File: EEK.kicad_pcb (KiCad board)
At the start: 2 copper layers, 165 x 51.8 mm, 35 parts

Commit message: add PCB features
Add PCB deatures un PCB Editor
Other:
- board text added: "0,0000 mm / 0,0000 mm"
- board text added: "0,3000 mm"
- board text added: "1,6000 mm"
- board text added: "165,0000 mm x 51,7500 mm"
- board text added: "2"
- board text added: "CARACTÉRISTIQUES du PCB"
- board text added: "Connecteurs de bord de cartes:"
- board text added: "Contour du PCB Métallisé:"
- board text added: "Contrôle d'Impédance:"
- board text added: "Diamètre de trou min:"
- board text added: "Dimensions hors tout PCB:"
- board text added: "Epaisseur du PCB:"
- board text added: "Finition Cuivre:"
- board text added: "Nombre de Couches Cuivre:"
- board text added: "Non"
- board text added: "None"
- board text added: "Pads castellated:"
- board text added: "Piste / espacement min:"

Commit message: fix the bug on OLED power supply pin1 and 2 inverted (3.3V and GND)
Fix the bug on the OLED power supply pins which have been inverted PIN 1 3.3V and pin 2 GND
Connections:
- U10 pad 1: GND -> /3.3V
- U10 pad 2: /3.3V -> GND
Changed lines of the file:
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@@
 			)
 		)
+		(sheetname "Racine")
+		(sheetfile "EEK.kicad_sch")
 		(attr through_hole)
 		(fp_line
@@
 			)
 		)
+		(property ki_fp_filters "R_*")
+		(sheetname "Racine")
+		(sheetfile "EEK.kicad_sch")
 		(attr through_hole)
 		(fp_line
@@
 			)
 		)
+		(property ki_fp_filters "Pin* Test*")
+		(sheetname "Racine")
+		(sheetfile "EEK.kicad_sch")
 		(attr exclude_from_pos_files)
 		(fp_circle
@@
 			)
 		)
+		(property ki_fp_filters "Pin* Test*")
+		(sheetname "Racine")
+		(sheetfile "EEK.kicad_sch")
 		(attr exclude_from_pos_files)
 		(fp_circle
@@
 			)
 		)
+		(property ki_fp_filters "LED* LED_SMD:* LED_THT:*")
+		(sheetname "Racine")
+		(sheetfile "EEK.kicad_sch")
 		(attr through_hole)
 		(fp_line
@@
 			)
 		)
+		(property ki_fp_filters "Pin* Test*")
+		(sheetname "Racine")
+		(sheetfile "EEK.kicad_sch")
 		(attr exclude_from_pos_files)
 		(fp_circle
@@
 			)
 		)
+		(property ki_fp_filters "R_*")
+		(sheetname "Racine")
+		(sheetfile "EEK.kicad_sch")
 		(attr through_hole)
 		(fp_line
@@
 			)
 		)
+		(property ki_fp_filters "LED* LED_SMD:* LED_THT:*")
+		(sheetname "Racine")
+		(sheetfile "EEK.kicad_sch")
 		(attr through_hole)
 		(fp_line
@@
 			)
 		)
+		(property ki_fp_filters "Pin* Test*")
+		(sheetname "Racine")
+		(sheetfile "EEK.kicad_sch")
 		(attr exclude_from_pos_files)
 		(fp_circle
@@
 			)
 		)
+		(sheetname "Racine")
+		(sheetfile "EEK.kicad_sch")
 		(attr through_hole)
 		(fp_rect
@@
 			)
 		)
+		(sheetname "Racine")
+		(sheetfile "EEK.kicad_sch")
 		(attr through_hole)
 		(fp_line
@@
 			(layers "*.Cu" "*.Mask")
 			(remove_unused_layers no)
-			(net 49 "GND")
-			(pinfunction "GND")
+			(net 26 "/3.3V")
+			(pinfunction "VDD")
 			(pintype "passive")
 		)
@@
 			(layers "*.Cu" "*.Mask")
 			(remove_unused_layers no)
-			(net 26 "/3.3V")
-			(pinfunction "VDD")
+			(net 49 "GND")
+			(pinfunction "GND")
 			(pintype "passive")
 		)
@@
 			)
 		)
+		(property ki_fp_filters "LED* LED_SMD:* LED_THT:*")
+		(sheetname "Racine")
+		(sheetfile "EEK.kicad_sch")
 		(attr through_hole)
 		(fp_line
@@
 			)
 		)
+		(property ki_fp_filters "Pin* Test*")
+		(sheetname "Racine")
+		(sheetfile "EEK.kicad_sch")
 		(attr exclude_from_pos_files)
 		(fp_circle
@@
 			)
 		)
+		(property ki_fp_filters "LED* LED_SMD:* LED_THT:*")
+		(sheetname "Racine")
+		(sheetfile "EEK.kicad_sch")
 		(attr through_hole)
 		(fp_line
@@
 			)
 		)
+		(property ki_fp_filters "LED* LED_SMD:* LED_THT:*")
+		(sheetname "Racine")
+		(sheetfile "EEK.kicad_sch")
 		(attr through_hole)
 		(fp_line
@@
 			)
 		)
+		(property ki_fp_filters "Pin* Test*")
+		(sheetname "Racine")
+		(sheetfile "EEK.kicad_sch")
 		(attr exclude_from_pos_files)
 		(fp_circle
@@
 			)
 		)
+		(property ki_fp_filters "Pin* Test*")
+		(sheetname "Racine")
+		(sheetfile "EEK.kicad_sch")
 		(attr exclude_from_pos_files)
 		(fp_circle
@@
 			)
 		)
+		(property ki_fp_filters "Pin* Test*")
+		(sheetname "Racine")
+		(sheetfile "EEK.kicad_sch")
 		(attr exclude_from_pos_files)
 		(fp_circle
@@
 			)
 		)
+		(sheetname "Racine")
+		(sheetfile "EEK.kicad_sch")
 		(attr through_hole)
 		(fp_line
@@
 			)
 		)
+		(property ki_fp_filters "LED* LED_SMD:* LED_THT:*")
+		(sheetname "Racine")
+		(sheetfile "EEK.kicad_sch")
 		(attr through_hole)
 		(fp_line
@@
 			)
 		)
+		(sheetname "Racine")
+		(sheetfile "EEK.kicad_sch")
 		(attr through_hole)
 		(fp_line
@@
 			)
 		)
+		(sheetname "Racine")
+		(sheetfile "EEK.kicad_sch")
 		(attr through_hole)
 		(fp_line
@@
 			)
 		)
+		(property ki_fp_filters "Pin* Test*")
+		(sheetname "Racine")
+		(sheetfile "EEK.kicad_sch")
 		(attr exclude_from_pos_files)
 		(fp_circle
@@
 			)
 		)
+		(sheetname "Racine")
+		(sheetfile "EEK.kicad_sch")
 		(attr through_hole)
 		(fp_line
@@
 			)
 		)
+		(property ki_fp_filters "Pin* Test*")
+		(sheetname "Racine")
+		(sheetfile "EEK.kicad_sch")
 		(attr exclude_from_pos_files)
 		(fp_circle
@@
 			)
 		)
+		(property ki_fp_filters "R_*")
+		(sheetname "Racine")
+		(sheetfile "EEK.kicad_sch")
 		(attr through_hole)
 		(fp_line
@@
 			)
 		)
+		(property ki_fp_filters "R_*")
+		(sheetname "Racine")
+		(sheetfile "EEK.kicad_sch")
 		(attr through_hole)
 		(fp_line
@@
 			)
 		)
+		(property ki_fp_filters "Pin* Test*")
+		(sheetname "Racine")
+		(sheetfile "EEK.kicad_sch")
 		(attr exclude_from_pos_files)
 		(fp_circle
@@
 			)
 		)
+		(property ki_fp_filters "R_*")
+		(sheetname "Racine")
+		(sheetfile "EEK.kicad_sch")
 		(attr through_hole)
 		(fp_line
@@
 			)
 		)
+		(property ki_fp_filters "Pin* Test*")
+		(sheetname "Racine")
+		(sheetfile "EEK.kicad_sch")
 		(attr exclude_from_pos_files)
 		(fp_circle
@@
 			)
 		)
+		(sheetname "Racine")
+		(sheetfile "EEK.kicad_sch")
 		(attr through_hole)
 		(fp_line
@@
 			)
 		)
+		(property ki_fp_filters "R_*")
+		(sheetname "Racine")
+		(sheetfile "EEK.kicad_sch")
 		(attr through_hole)
 		(fp_line
@@
 			)
 		)
+		(sheetname "Racine")
+		(sheetfile "EEK.kicad_sch")
 		(attr through_hole)
 		(fp_line
@@
 			)
 		)
+		(property ki_fp_filters "Pin* Test*")
+		(sheetname "Racine")
+		(sheetfile "EEK.kicad_sch")
 		(attr exclude_from_pos_files)
 		(fp_circle

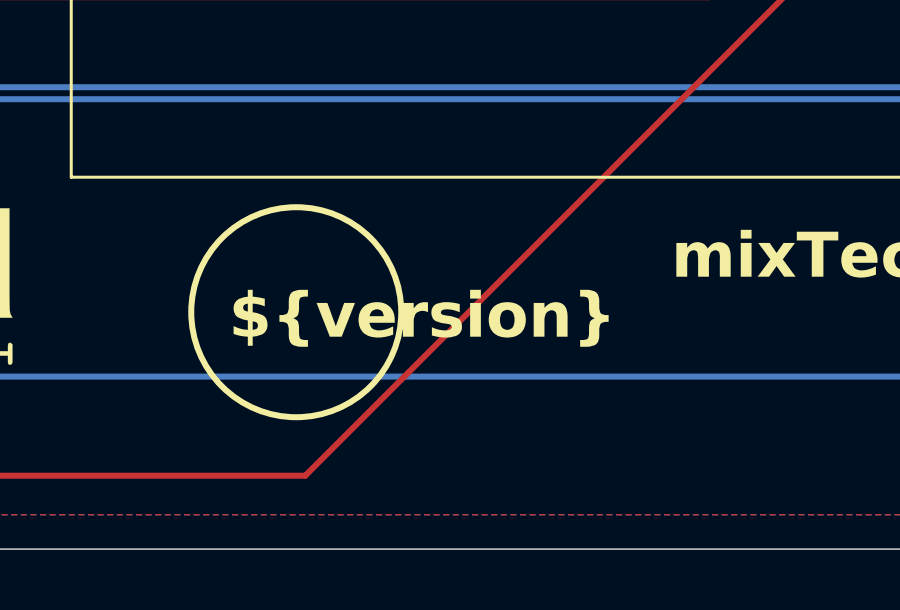
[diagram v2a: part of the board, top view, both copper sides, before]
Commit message: update version number V1.1
update version number to 1.1
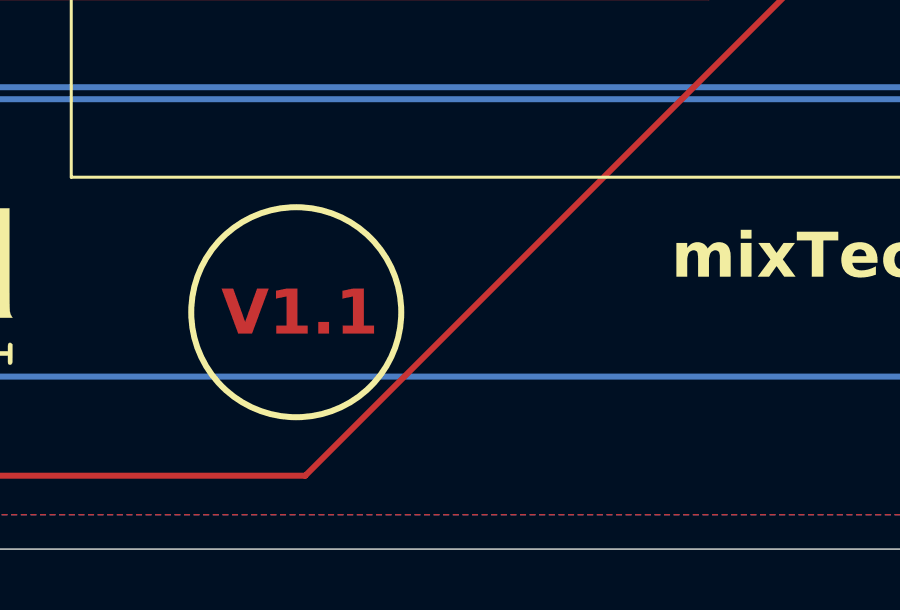
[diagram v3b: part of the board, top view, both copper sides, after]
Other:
- board text added: "V1.1"
- board text removed: "${version}"
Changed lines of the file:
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@@
 	(property "compagny" "mixTech")
 	(property "title" "PCB EEK for ESP32-WROOM-32")
-	(property "version" "V1.0")
+	(property "version" "V1.1")
 	(net 0 "")
 	(net 1 "/GFL")
@@
 		(layer "Edge.Cuts")
 	)
+	(gr_text "V1.1"
+		(at 146.25 121.5 0)
+		(layer "F.Cu")
+		(effects
+			(font
+				(size 1.5 1.5)
+				(thickness 0.3)
+				(bold yes)
+			)
+			(justify left bottom)
+		)
+	)
 	(gr_text "-"
 		(at 94.25 101.6041 0)
@@
 		)
 	)
-	(gr_text "${version}"
+	(gr_text "\n\n"
 		(at 146.5 121.6041 0)
 		(layer "F.SilkS")

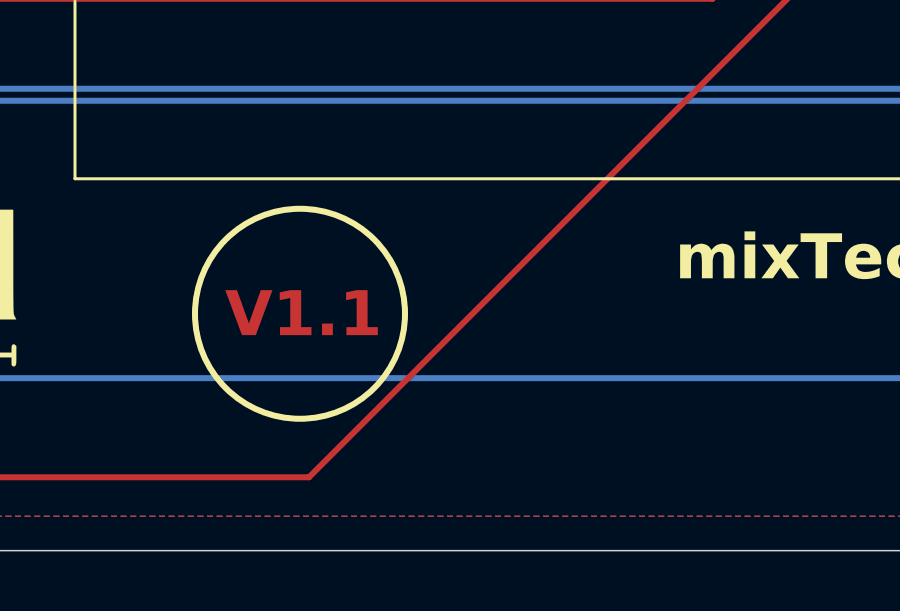
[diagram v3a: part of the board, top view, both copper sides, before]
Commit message: fix bug with version number on pcb ${version}
fix bug with version number on pcb ${version}
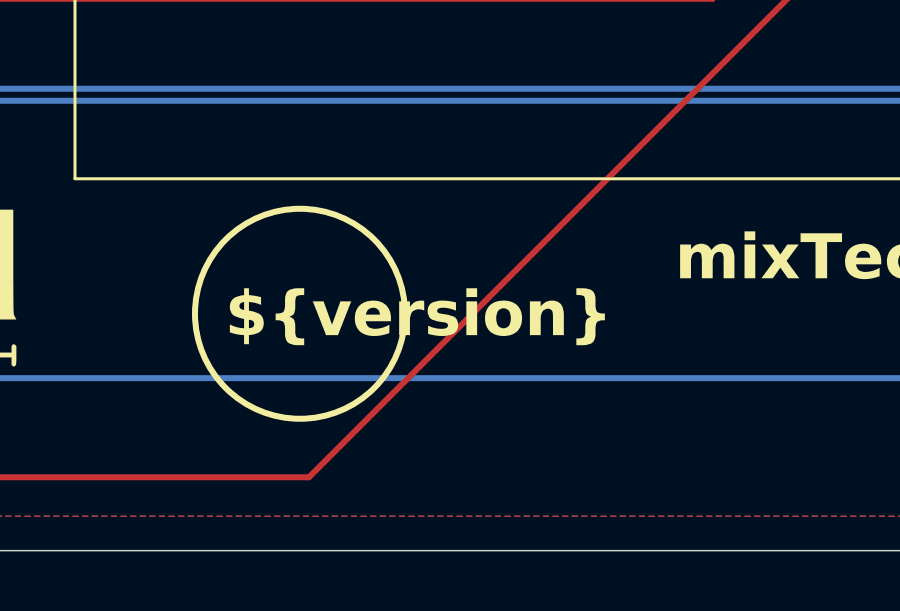
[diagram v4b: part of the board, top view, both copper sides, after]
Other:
- board text added: "${version}"
- board text removed: "V1.1"
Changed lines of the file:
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@@
 		(layer "Edge.Cuts")
-	)
-	(gr_text "V1.1"
-		(at 146.25 121.5 0)
-		(layer "F.Cu")
-		(effects
-			(font
-				(size 1.5 1.5)
-				(thickness 0.3)
-				(bold yes)
-			)
-			(justify left bottom)
-		)
 	)
 	(gr_text "-"
@@
 		(layer "F.SilkS")
 		(effects
+			(font
+				(size 1.5 1.5)
+				(thickness 0.3)
+				(bold yes)
+			)
+			(justify left bottom)
+		)
+	)
+	(gr_text "${version}"
+		(at 146.25 121.5 0)
+		(layer "F.SilkS")
+		(effects

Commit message: change the footprint of the tactil switch which was not correct
Change the footprint of the tactil switch which was not correct
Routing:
- net /CW: track 164.2 -> 146.4 mm, vias 0 -> 1
- net /Up: track 113.1 -> 121.7 mm
- net /Kill: track 122.1 -> 129.4 mm
- net /CCw: track 133.2 -> 140.5 mm
- net /Takeoff: track 174.4 -> 181.7 mm
- net /Down: track 157.9 -> 159.7 mm

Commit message: Change the direction of the MCU6050 connector
Change the direction of the MCU6050 connector pin 1 to pin 8
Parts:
- moved U9 17.8 mm to (136.1, 83.3), turned to -90 degrees
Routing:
- net /SCL: track 109.0 -> 119.1 mm
- net /SDA: track 117.7 -> 116.2 mm
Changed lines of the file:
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@@
 	(footprint "Connector_PinHeader_2.54mm:PinHeader_1x08_P2.54mm_Vertical"
 		(layer "F.Cu")
-		(at 118.38 83.284118 90)
+		(at 136.13 83.284118 -90)
 		(descr "Through hole straight pin header, 1x08, 2.54mm pitch, single row")
 		(tags "Through hole pin header THT 1x08 2.54mm single row")
 		(property "Reference" "U9"
-			(at 0 -2.63 -90)
+			(at 0 -2.63 90)
 			(layer "F.SilkS")
 			(effects
@@
 		)
 		(property "Value" "~"
-			(at 0 20.11 -90)
+			(at 0 20.11 90)
 			(layer "F.Fab")
 			(effects
@@
 		)
 		(property "Footprint" "Connector_PinHeader_2.54mm:PinHeader_1x08_P2.54mm_Vertical"
-			(at 0 0 90)
+			(at 0 0 -90)
 			(unlocked yes)
 			(layer "F.Fab")
@@
 		)
 		(property "Datasheet" ""
-			(at 0 0 90)
+			(at 0 0 -90)
 			(unlocked yes)
 			(layer "F.Fab")
@@
 		)
 		(property "Description" "MPU6050 (GY-521)"
-			(at 0 0 90)
+			(at 0 0 -90)
 			(unlocked yes)
 			(layer "F.Fab")
@@
 		(attr through_hole)
 		(fp_line
-			(start -1.33 -1.33)
-			(end 0 -1.33)
+			(start -1.33 19.11)
+			(end 1.33 19.11)
 			(stroke
 				(width 0.12)
@@
 		)
 		(fp_line
-			(start -1.33 0)
-			(end -1.33 -1.33)
+			(start -1.33 1.27)
+			(end -1.33 19.11)
 			(stroke
 				(width 0.12)
@@
 		)
 		(fp_line
-			(start 1.33 1.27)
-			(end 1.33 19.11)
+			(start -1.33 1.27)
+			(end 1.33 1.27)
 			(stroke
 				(width 0.12)
@@
 		)
 		(fp_line
-			(start -1.33 1.27)
-			(end 1.33 1.27)
+			(start 1.33 1.27)
+			(end 1.33 19.11)
 			(stroke
 				(width 0.12)
@@
 		)
 		(fp_line
-			(start -1.33 1.27)
-			(end -1.33 19.11)
+			(start -1.33 0)
+			(end -1.33 -1.33)
 			(stroke
 				(width 0.12)
@@
 		)
 		(fp_line
-			(start -1.33 19.11)
-			(end 1.33 19.11)
+			(start -1.33 -1.33)
+			(end 0 -1.33)
 			(stroke
 				(width 0.12)
@@
 		)
 		(fp_line
-			(start 1.8 -1.8)
-			(end -1.8 -1.8)
+			(start -1.8 19.55)
+			(end 1.8 19.55)
 			(stroke
 				(width 0.05)
@@
 		)
 		(fp_line
-			(start -1.8 -1.8)
-			(end -1.8 19.55)
+			(start 1.8 19.55)
+			(end 1.8 -1.8)
 			(stroke
 				(width 0.05)
@@
 		)
 		(fp_line
-			(start 1.8 19.55)
-			(end 1.8 -1.8)
+			(start -1.8 -1.8)
+			(end -1.8 19.55)
 			(stroke
 				(width 0.05)
@@
 		)
 		(fp_line
-			(start -1.8 19.55)
-			(end 1.8 19.55)
+			(start 1.8 -1.8)
+			(end -1.8 -1.8)
 			(stroke
 				(width 0.05)
@@
 		)
 		(fp_line
-			(start 1.27 -1.27)
-			(end 1.27 19.05)
+			(start -1.27 19.05)
+			(end -1.27 -0.635)
 			(stroke
 				(width 0.1)
@@
 		)
 		(fp_line
-			(start -0.635 -1.27)
-			(end 1.27 -1.27)
+			(start 1.27 19.05)
+			(end -1.27 19.05)
 			(stroke
 				(width 0.1)
@@
 		)
 		(fp_line
-			(start 1.27 19.05)
-			(end -1.27 19.05)
+			(start -0.635 -1.27)
+			(end 1.27 -1.27)
 			(stroke
 				(width 0.1)
@@
 		)
 		(fp_line
-			(start -1.27 19.05)
-			(end -1.27 -0.635)
+			(start 1.27 -1.27)
+			(end 1.27 19.05)
 			(stroke
 				(width 0.1)
@@
 		)
 		(fp_text user "${REFERENCE}"
-			(at 0 8.89 0)
+			(at 0 8.89 180)
 			(layer "F.Fab")
 			(effects
@@
 		)
 		(pad "1" thru_hole rect
-			(at 0 0 90)
+			(at 0 0 270)
 			(size 1.7 1.7)
 			(drill 1)
@@
 		)
 		(pad "2" thru_hole oval
-			(at 0 2.54 90)
+			(at 0 2.54 270)
 			(size 1.7 1.7)
 			(drill 1)
@@
 		)
 		(pad "3" thru_hole oval
-			(at 0 5.08 90)
+			(at 0 5.08 270)
 			(size 1.7 1.7)
 			(drill 1)
@@
 		)
 		(pad "4" thru_hole oval
-			(at 0 7.62 90)
+			(at 0 7.62 270)
 			(size 1.7 1.7)
 			(drill 1)
@@
 		)
 		(pad "5" thru_hole oval
-			(at 0 10.16 90)
+			(at 0 10.16 270)
 			(size 1.7 1.7)
 			(drill 1)
@@
 		)
 		(pad "6" thru_hole oval
-			(at 0 12.7 90)
+			(at 0 12.7 270)
 			(size 1.7 1.7)
 			(drill 1)
@@
 		)
 		(pad "7" thru_hole oval
-			(at 0 15.24 90)
+			(at 0 15.24 270)
 			(size 1.7 1.7)
 			(drill 1)
@@
 		)
 		(pad "8" thru_hole oval
-			(at 0 17.78 90)
+			(at 0 17.78 270)
 			(size 1.7 1.7)
 			(drill 1)
@@
 	)
 	(segment
-		(start 123.46 88.571817)
+		(start 160.33 82.1041)
+		(end 160.33 83.3541)
+		(width 0.2)
+		(layer "F.Cu")
+		(net 50)
+	)
+	(segment
+		(start 112.5 112.1041)
 		(end 112.5 99.531817)
 		(width 0.2)
@@
 	)
 	(segment
-		(start 160.33 82.1041)
-		(end 160.33 83.3541)
+		(start 127.765882 80)
+		(end 131.05 83.284118)
+		(width 0.2)
+		(layer "F.Cu")
+		(net 50)
+	)
+	(segment
+		(start 112.5 99.531817)
+		(end 115.75 96.281817)
 		(width 0.2)
 		(layer "F.Cu")
@@
 	)
 	(segment
-		(start 112.5 99.531817)
-		(end 112.5 112.1041)
+		(start 117 80)
+		(end 127.765882 80)
+		(width 0.2)
+		(layer "F.Cu")
+		(net 50)
+	)
+	(segment
+		(start 115.75 81.25)
+		(end 117 80)
 		(width 0.2)
 		(layer "F.Cu")
@@
 	)
 	(segment
-		(start 123.46 83.284118)
-		(end 123.46 88.571817)
+		(start 115.75 96.281817)
+		(end 115.75 81.25)
 		(width 0.2)
 		(layer "F.Cu")
@@
 	(segment
 		(start 132.75 78.8041)
-		(end 129.55 78.8041)
+		(end 132.25 79.3041)
 		(width 0.2)
 		(layer "B.Cu")
@@
 	)
 	(segment
-		(start 129.55 78.8041)
-		(end 126.75 81.6041)
+		(start 132.25 82.084118)
+		(end 131.05 83.284118)
 		(width 0.2)
 		(layer "B.Cu")
@@
 	)
 	(segment
-		(start 126.75 81.6041)
-		(end 125.140018 81.6041)
-		(width 0.2)
-		(layer "B.Cu")
-		(net 50)
-	)
-	(segment
 		(start 84.82 111.6741)
 		(end 112.07 111.6741)
@@
 	)
 	(segment
-		(start 125.140018 81.6041)
-		(end 123.46 83.284118)
+		(start 132.25 79.3041)
+		(end 132.25 82.084118)
 		(width 0.2)
 		(layer "B.Cu")
@@
 	)
 	(segment
-		(start 127.219982 84.5041)
-		(end 150.15 84.5041)
+		(start 126 85.794118)
+		(end 128.51 83.284118)
 		(width 0.2)
 		(layer "F.Cu")
@@
 	)
 	(segment
-		(start 113 99.597503)
-		(end 126 86.597503)
+		(start 126 86.597503)
+		(end 126 85.794118)
 		(width 0.2)
 		(layer "F.Cu")
@@
 	)
 	(segment
-		(start 71.7375 114.0541)
-		(end 74.9375 110.8541)
+		(start 113 99.597503)
+		(end 126 86.597503)
 		(width 0.2)
 		(layer "F.Cu")
@@
 	)
 	(segment
-		(start 150.15 84.5041)
-		(end 152.25 86.6041)
+		(start 152.25 86.6041)
+		(end 131.829982 86.6041)
 		(width 0.2)
 		(layer "F.Cu")
@@
 	)
 	(segment
-		(start 126 83.284118)
-		(end 127.219982 84.5041)
+		(start 71.7375 114.0541)
+		(end 74.9375 110.8541)
 		(width 0.2)
 		(layer "F.Cu")
@@
 	)
 	(segment
-		(start 126 86.597503)
-		(end 126 83.284118)
+		(start 131.829982 86.6041)
+		(end 128.51 83.284118)
 		(width 0.2)
 		(layer "F.Cu")

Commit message: add project name EEK on the silkscreen layer
Add project name "EEK" on the silkscreen layer
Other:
- board text added: "EEK"
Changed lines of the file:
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@@
+		)
+	)
+	(gr_text "EEK "
+		(at 162 124 0)
+		(layer "F.SilkS")
+		(effects
+			(font
+				(size 2 2)
+				(thickness 0.2)
+			)
+			(justify left bottom)
 		)
 	)
